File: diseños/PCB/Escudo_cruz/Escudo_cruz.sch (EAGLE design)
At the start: 12 parts, among them X1 TERMINAL-BLOCK-3.5MM-3-PIN-RO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, X2 TERMINAL-BLOCK-3.5MM-3-PIN-RO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, X3 TERMINAL-BLOCK-3.5MM-3-PIN-RO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, X4 TERMINAL-BLOCK-3.5MM-3-PIN-RO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

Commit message: Cortes Mes y Año
Grupo tres capa 1 y 3
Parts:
- added SW1: (no value), adafruit:SWITCH_PUSHBUTTONSOFTTOUCHSMD_SJ
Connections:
- new net N$5: SW1.P$1, U$3.RST
- net GND: now also SW1.P$2
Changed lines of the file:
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@@
 <part name="+5V_3" library="solpad" library_urn="urn:adsk.eagle:library:364" deviceset="LSP10" device="" package3d_urn="urn:adsk.eagle:package:26501/1"/>
 <part name="GND9" library="supply1" library_urn="urn:adsk.eagle:library:371" deviceset="GND" device=""/>
+<part name="SW1" library="adafruit" library_urn="urn:adsk.eagle:library:420" deviceset="SWITCH_PUSHBUTTON" device="SOFTTOUCHSMD_SJ" package3d_urn="urn:adsk.eagle:package:6240956/1"/>
+<part name="GND10" library="supply1" library_urn="urn:adsk.eagle:library:371" deviceset="GND" device=""/>
 </parts>
 <sheets>
@@
 <attribute name="VALUE" x="-55.88" y="35.56" size="1.778" layer="96"/>
 </instance>
+<instance part="SW1" gate="G$1" x="-15.24" y="104.14" smashed="yes">
+<attribute name="NAME" x="-17.78" y="107.696" size="1.27" layer="95"/>
+<attribute name="VALUE" x="-17.78" y="101.854" size="1.27" layer="96"/>
+</instance>
+<instance part="GND10" gate="1" x="2.54" y="101.6" smashed="yes">
+<attribute name="VALUE" x="0" y="99.06" size="1.778" layer="96"/>
+</instance>
 </instances>
 <busses>
@@
 <wire x1="-53.34" y1="40.64" x2="-53.34" y2="43.18" width="0.1524" layer="91"/>
 </segment>
+<segment>
+<pinref part="GND10" gate="1" pin="GND"/>
+<pinref part="SW1" gate="G$1" pin="P$2"/>
+<wire x1="2.54" y1="104.14" x2="-10.16" y2="104.14" width="0.1524" layer="91"/>
+</segment>
 </net>
 <net name="GND@1" class="0">
@@
 </segment>
 </net>
+<net name="N$5" class="0">
+<segment>
+<pinref part="U$3" gate="G$1" pin="RST"/>
+<wire x1="-33.02" y1="93.98" x2="-22.86" y2="93.98" width="0.1524" layer="91"/>
+<pinref part="SW1" gate="G$1" pin="P$1"/>
+<wire x1="-22.86" y1="93.98" x2="-22.86" y2="104.14" width="0.1524" layer="91"/>
+<wire x1="-22.86" y1="104.14" x2="-20.32" y2="104.14" width="0.1524" layer="91"/>
+</segment>
+</net>

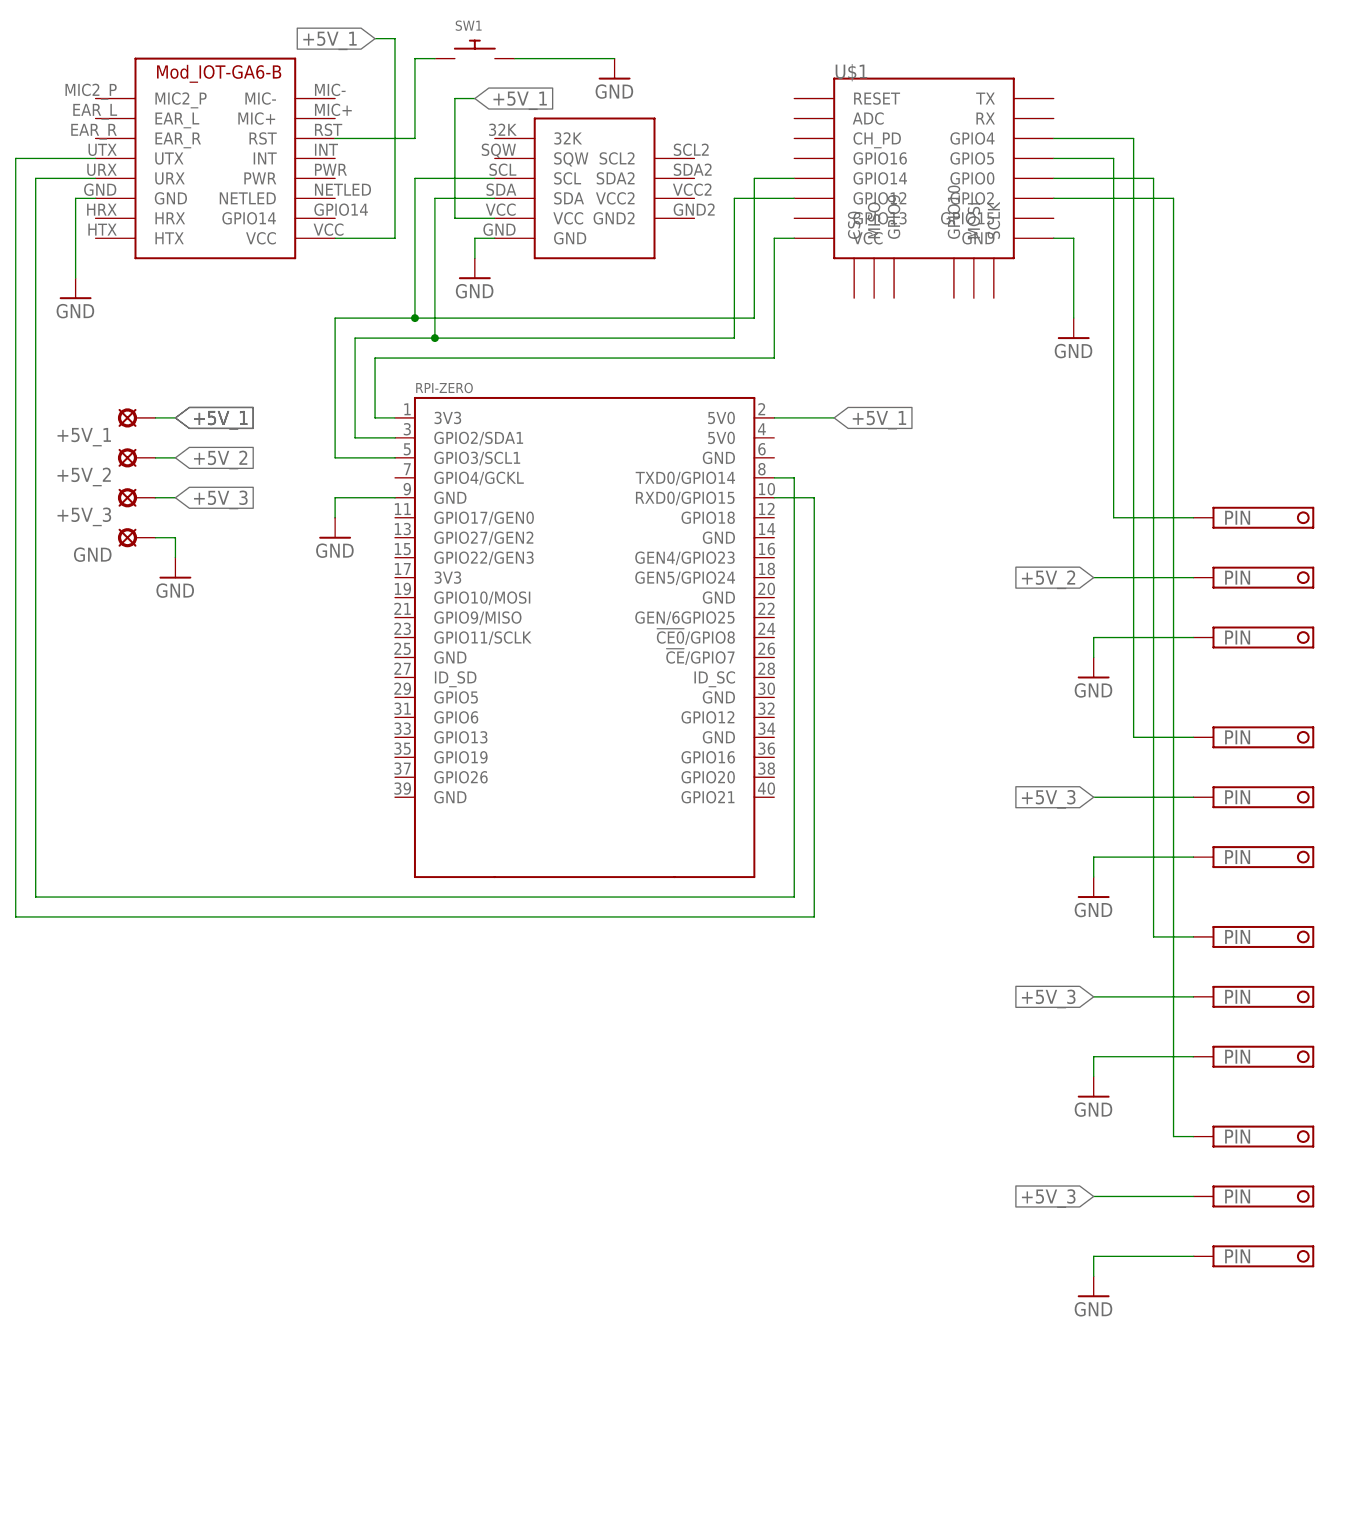
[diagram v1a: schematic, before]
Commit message: Modificaciones SHIELD raspberry
Se descarta la idea de la comunicación I2C y se agrega una quinta salida de display para indicar la tonalidad del tipo de accidente.
Cambios a los cortes del grupo 2 capas 1, 2 y 3
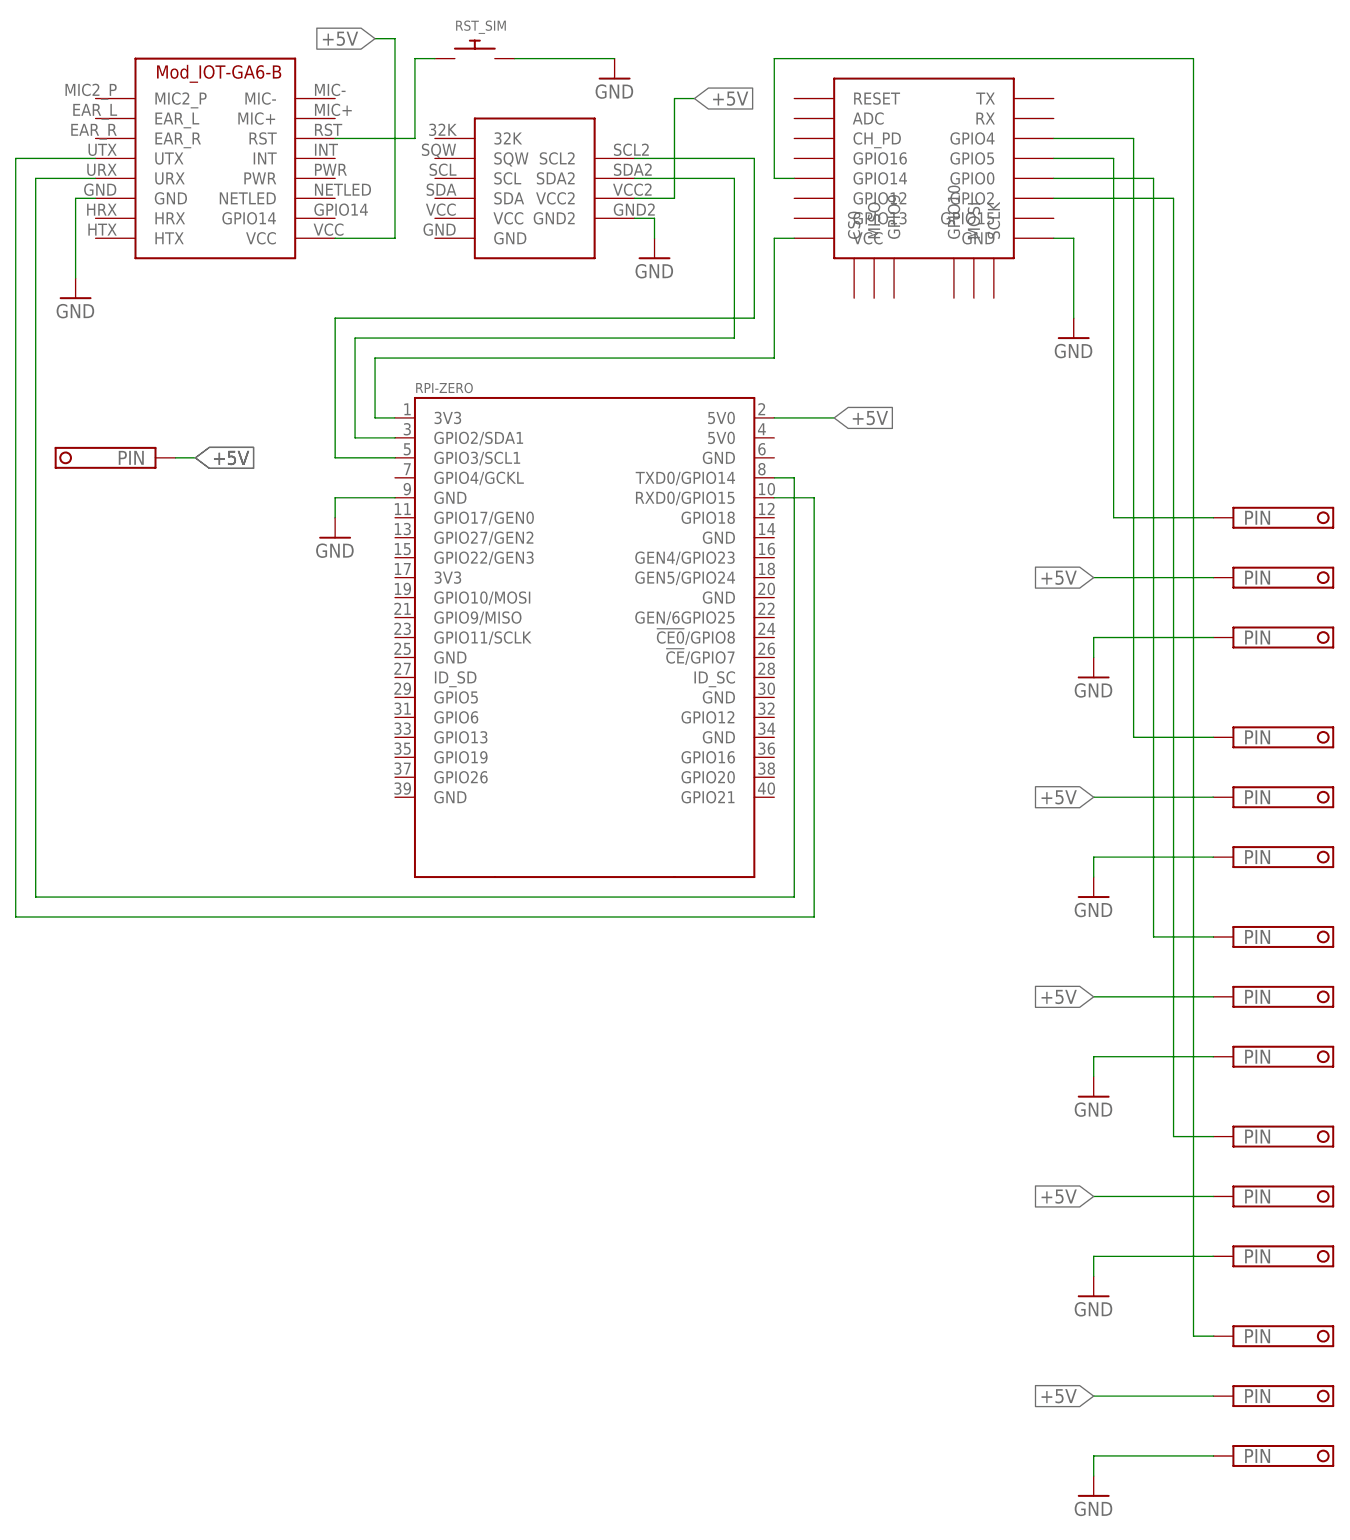
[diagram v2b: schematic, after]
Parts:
- removed +5V_1, +5V_2, +5V_3, GND: LSP10, solpad:LSP10
- removed X1, X2, X3, X4: TERMINAL-BLOCK-3.5MM-3-PIN-ROUND-PAD, Rembrandt Electronics - Terminal Block 3-5mm v1-0:TERMINAL-BLOCK-3.5MM-3-PIN-ROUND-PAD
- added AÑO, CRUZ, DÍAZ, INDICADOR, MES: TERMINAL-BLOCK-3.5MM-3-PIN-ROUND-PAD, Rembrandt Electronics - Terminal Block 3-5mm v1-0:TERMINAL-BLOCK-3.5MM-3-PIN-ROUND-PAD
- added POWER: TERMINAL-BLOCK-3.5MM-2-PIN-ROUND-PAD, Rembrandt Electronics - Terminal Block 3-5mm v1-0:TERMINAL-BLOCK-3.5MM-2-PIN-ROUND-PAD
- renumbered SW1 to RST_SIM, U$1 to ESP8266, U$3 to SIM
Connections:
- removed net +5V_1: +5V_1.MP, SIM.VCC, U$2.5V0@1, U$4.VCC
- removed net +5V_2: +5V_2.MP, X1-2.VCC
- removed net +5V_3: +5V_3.MP, X2-2.VCC, X3-2.VCC, X4-2.VCC
- new net +5V: AÑO-2.VCC, CRUZ-2.VCC, DÍAZ-2.VCC, MES-2.VCC, POWER-1.VCC, SIM.VCC, U$2.5V0@1
- new net N$10: U$4.VCC2
- new net N$6: INDICADOR-2.VCC
- new net N$9: ESP8266.GPIO14, INDICADOR-1.VCC
- net GND: now also AÑO-3.VCC, CRUZ-3.VCC, DÍAZ-3.VCC, INDICADOR-3.VCC, MES-3.VCC, U$4.GND2; no longer GND.MP, U$4.GND, X1-3.VCC, X2-3.VCC, X3-3.VCC, X4-3.VCC
- net N$12: now also DÍAZ-1.VCC; no longer X2-1.VCC
- net N$13: now also MES-1.VCC; no longer X3-1.VCC
- net N$14: now also AÑO-1.VCC; no longer X4-1.VCC
- net N$3: now also U$4.SDA2; no longer ESP8266.GPIO12, U$4.SDA
- net N$4: now also U$4.SCL2; no longer ESP8266.GPIO14, U$4.SCL
- net N$7: now also CRUZ-1.VCC; no longer X1-1.VCC
